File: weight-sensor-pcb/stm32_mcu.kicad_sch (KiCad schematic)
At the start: 18 parts, among them J1 TC2030, J4 Conn_01x05_Pin, U4 STM32F042F4P6

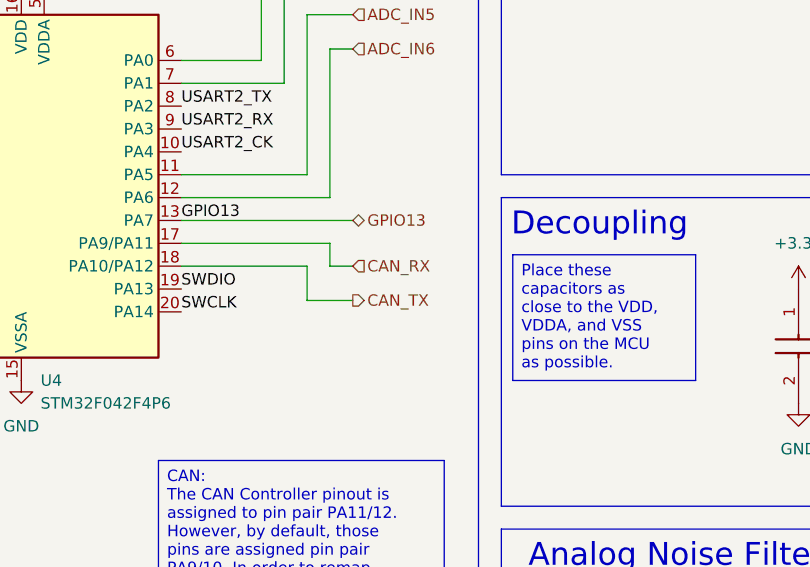
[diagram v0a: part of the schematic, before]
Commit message: update CAN transceiver schematic/layout, use env vars for library paths
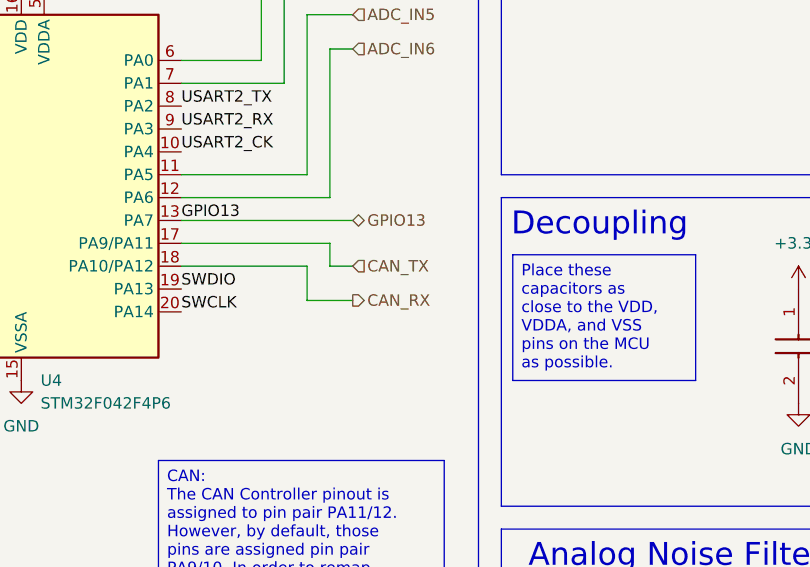
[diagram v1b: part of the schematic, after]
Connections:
- net CAN_RX: now also U4.18 (PA10/PA12); no longer U4.17 (PA9/PA11)
- net CAN_TX: now also U4.17 (PA9/PA11); no longer U4.18 (PA10/PA12)
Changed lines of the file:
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@@
 		)
 	)
-	(hierarchical_label "CAN_TX"
+	(hierarchical_label "CAN_RX"
 		(shape output)
 		(at 185.42 99.06 0)
@@
 		)
 	)
-	(hierarchical_label "CAN_RX"
+	(hierarchical_label "CAN_TX"
 		(shape input)
 		(at 185.42 95.25 0)

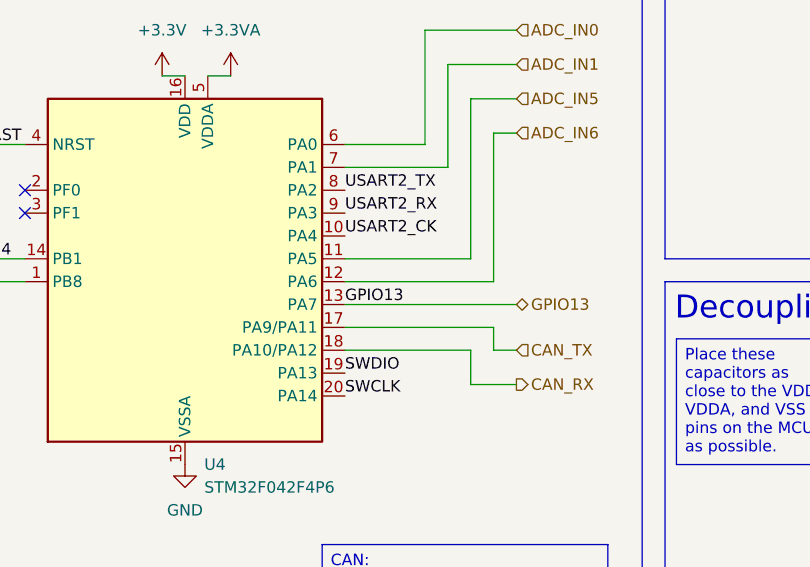
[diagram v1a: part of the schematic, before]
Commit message: Add backup USB power
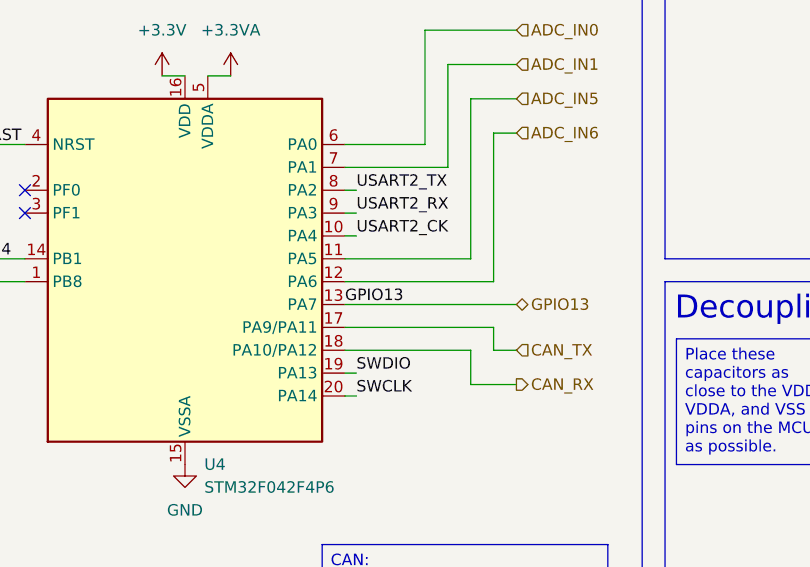
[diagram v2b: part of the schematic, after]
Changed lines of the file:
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@@
+	(wire
+		(pts
+			(xy 167.64 100.33) (xy 166.37 100.33)
+		)
+		(stroke
+			(width 0)
+			(type default)
+		)
+	)
 	(wire
 		(pts
@@
 	(wire
 		(pts
+			(xy 167.64 77.47) (xy 166.37 77.47)
+		)
+		(stroke
+			(width 0)
+			(type default)
+		)
+	)
+	(wire
+		(pts
 			(xy 177.8 63.5) (xy 177.8 74.93)
 		)
@@
 	(wire
 		(pts
+			(xy 167.64 80.01) (xy 166.37 80.01)
+		)
+		(stroke
+			(width 0)
+			(type default)
+		)
+	)
+	(wire
+		(pts
 			(xy 180.34 95.25) (xy 166.37 95.25)
 		)
@@
 	(wire
 		(pts
+			(xy 167.64 97.79) (xy 166.37 97.79)
+		)
+		(stroke
+			(width 0)
+			(type default)
+		)
+	)
+	(wire
+		(pts
 			(xy 52.07 104.14) (xy 60.96 104.14)
 		)
@@
 		(pts
 			(xy 177.8 74.93) (xy 166.37 74.93)
+		)
+		(stroke
+			(width 0)
+			(type default)
+		)
+	)
+	(wire
+		(pts
+			(xy 167.64 82.55) (xy 166.37 82.55)
 		)
 		(stroke
@@
 	)
 	(label "USART2_TX"
-		(at 166.37 77.47 0)
+		(at 167.64 77.47 0)
 		(effects
 			(font
@@
 	)
 	(label "USART2_CK"
-		(at 166.37 82.55 0)
+		(at 167.64 82.55 0)
 		(effects
 			(font
@@
 	)
 	(label "USART2_RX"
-		(at 166.37 80.01 0)
+		(at 167.64 80.01 0)
 		(effects
 			(font
@@
 	)
 	(label "SWCLK"
-		(at 166.37 100.33 0)
+		(at 167.64 100.33 0)
 		(effects
 			(font
@@
 	)
 	(label "SWDIO"
-		(at 166.37 97.79 0)
-		(effects
-			(font
+		(at 167.64 97.79 0)
+		(effects
+			(font

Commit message: Layout draft complete
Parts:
- renumbered C5 to C8, C6 to C9, J4 to J5, J1 to J6, R8 to R21, TP9 to TP10, TP4 to TP11, TP5 to TP12, TP10 to TP13, TP2 to TP14, TP1 to TP15, TP3 to TP6, TP6 to TP7, TP7 to TP8, TP8 to TP9, U4 to U5
